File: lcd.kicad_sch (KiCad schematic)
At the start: 9 parts, among them J2 LCD 3.2" 240x320 Conn_01x14_P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, Q4 SI2301CDS-T1-GE3

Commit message: smaller caps remove ringing resistors
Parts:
- R14, R37, R38, R39: Manufacturer StackPole -> (none); Part # RMCF0603JT10K0 -> (none); VEND DIGI -> (none); VEND# RMCF0603JT10K0CT-ND -> (none)
- R3: LCSC C21190 -> C22775; Manufacturer StackPole -> (none); Part # RMCF0603JJ1K00 -> (none); VEND DIGI -> (none); VEND# RMCF0603JJ1K00CT-ND -> (none)
- R34: Manufacturer StackPole -> (none); Part # RMCF0603JJ1K00 -> (none); VEND DIGI -> (none); VEND# RMCF0603JJ1K00CT-ND -> (none)
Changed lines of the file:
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@@
 			)
 		)
-		(property "Part #" "RMCF0603JT10K0"
+		(property "Part #" ""
 			(at 77.47 -43.18 0)
 			(effects
@@
 			)
 		)
-		(property "VEND" "DIGI"
+		(property "VEND" ""
 			(at 77.47 -43.18 0)
 			(effects
@@
 			)
 		)
-		(property "VEND#" "RMCF0603JT10K0CT-ND"
+		(property "VEND#" ""
 			(at 77.47 -43.18 0)
 			(effects
@@
 			)
 		)
-		(property "Manufacturer" "StackPole"
+		(property "Manufacturer" ""
 			(at 77.47 -43.18 0)
 			(effects
@@
 			)
 		)
-		(property "LCSC" "C21190"
+		(property "LCSC" "C22775"
 			(at 119.38 104.14 0)
 			(effects
@@
 			)
 		)
-		(property "Manufacturer" "StackPole"
+		(property "Manufacturer" ""
 			(at 119.38 104.14 0)
 			(effects
@@
 			)
 		)
-		(property "Part #" "RMCF0603JJ1K00"
+		(property "Part #" ""
 			(at 119.38 104.14 0)
 			(effects
@@
 			)
 		)
-		(property "VEND" "DIGI"
+		(property "VEND" ""
 			(at 119.38 104.14 0)
 			(effects
@@
 			)
 		)
-		(property "VEND#" "RMCF0603JJ1K00CT-ND"
+		(property "VEND#" ""
 			(at 119.38 104.14 0)
 			(effects
@@
 			)
 		)
-		(property "Part #" "RMCF0603JT10K0"
+		(property "Part #" ""
 			(at 69.85 -60.96 0)
 			(effects
@@
 			)
 		)
-		(property "VEND" "DIGI"
+		(property "VEND" ""
 			(at 69.85 -60.96 0)
 			(effects
@@
 			)
 		)
-		(property "VEND#" "RMCF0603JT10K0CT-ND"
+		(property "VEND#" ""
 			(at 69.85 -60.96 0)
 			(effects
@@
 			)
 		)
-		(property "Manufacturer" "StackPole"
+		(property "Manufacturer" ""
 			(at 69.85 -60.96 0)
 			(effects
@@
 			)
 		)
-		(property "Part #" "RMCF0603JT10K0"
+		(property "Part #" ""
 			(at 16.51 8.89 0)
 			(effects
@@
 			)
 		)
-		(property "VEND" "DIGI"
+		(property "VEND" ""
 			(at 16.51 8.89 0)
 			(effects
@@
 			)
 		)
-		(property "VEND#" "RMCF0603JT10K0CT-ND"
+		(property "VEND#" ""
 			(at 16.51 8.89 0)
 			(effects
@@
 			)
 		)
-		(property "Manufacturer" "StackPole"
+		(property "Manufacturer" ""
 			(at 16.51 8.89 0)
 			(effects
@@
 			)
 		)
-		(property "Part #" "RMCF0603JT10K0"
+		(property "Part #" ""
 			(at 62.23 -60.96 0)
 			(effects
@@
 			)
 		)
-		(property "VEND" "DIGI"
+		(property "VEND" ""
 			(at 62.23 -60.96 0)
 			(effects
@@
 			)
 		)
-		(property "VEND#" "RMCF0603JT10K0CT-ND"
+		(property "VEND#" ""
 			(at 62.23 -60.96 0)
 			(effects
@@
 			)
 		)
-		(property "Manufacturer" "StackPole"
+		(property "Manufacturer" ""
 			(at 62.23 -60.96 0)
 			(effects
@@
 			)
 		)
-		(property "Manufacturer" "StackPole"
+		(property "Manufacturer" ""
 			(at 165.1 90.17 0)
 			(effects
@@
 			)
 		)
-		(property "Part #" "RMCF0603JJ1K00"
+		(property "Part #" ""
 			(at 165.1 90.17 0)
 			(effects
@@
 			)
 		)
-		(property "VEND" "DIGI"
+		(property "VEND" ""
 			(at 165.1 90.17 0)
 			(effects
@@
 			)
 		)
-		(property "VEND#" "RMCF0603JJ1K00CT-ND"
+		(property "VEND#" ""
 			(at 165.1 90.17 0)
 			(effects

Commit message: usb sheet
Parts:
- J2: now not fitted
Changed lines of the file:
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@@
 		(in_bom yes)
 		(on_board yes)
-		(dnp no)
+		(dnp yes)
 		(fields_autoplaced yes)
 		(property "Reference" "J2"

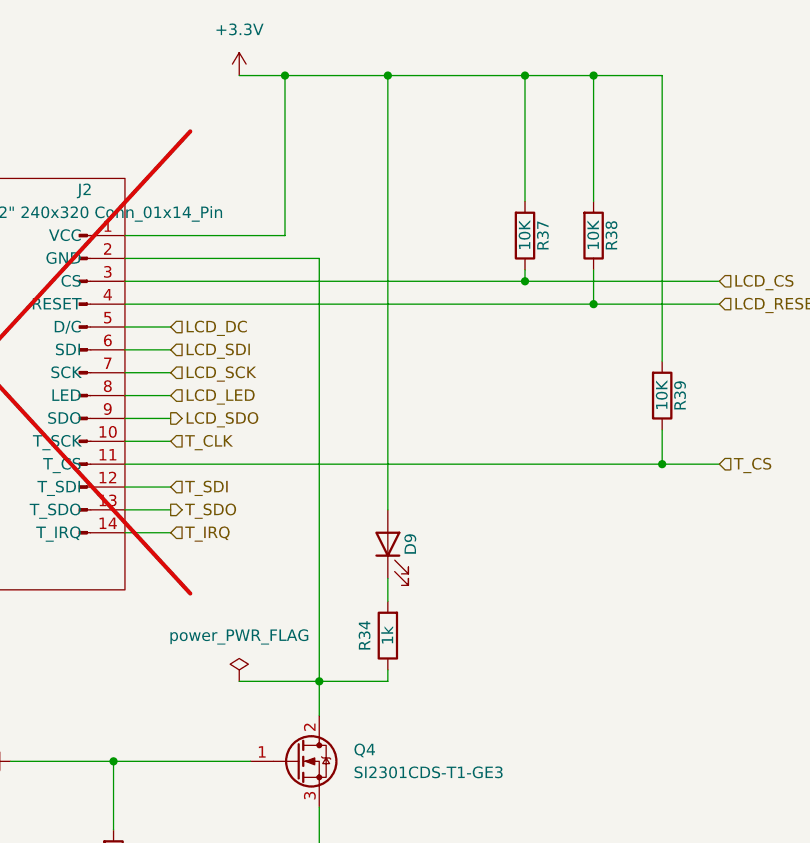
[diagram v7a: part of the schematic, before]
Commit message: smaller test pads
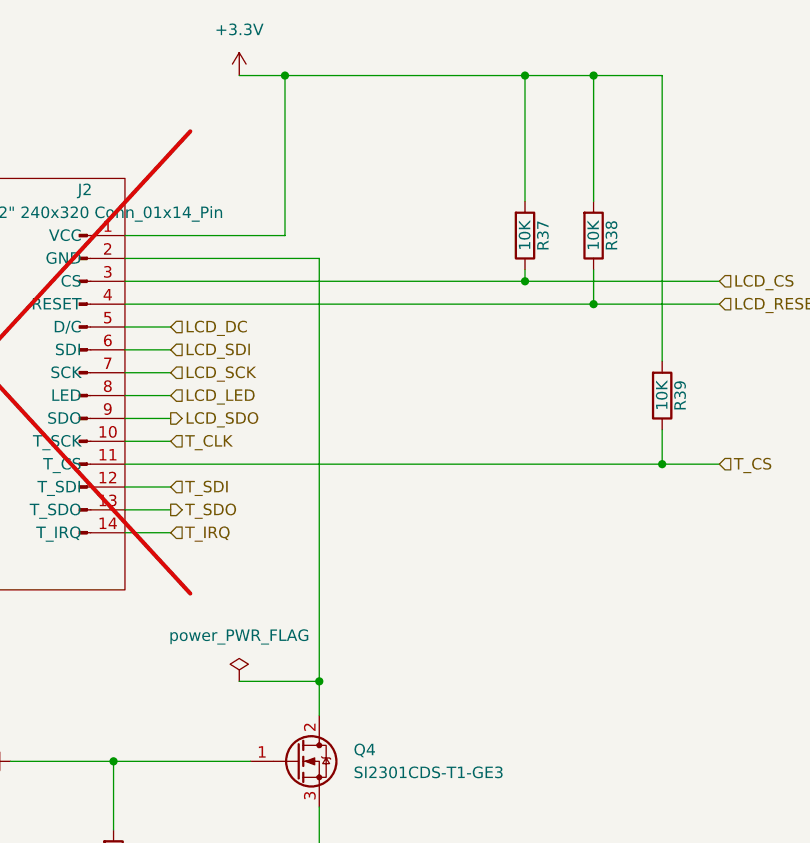
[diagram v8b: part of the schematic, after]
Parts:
- removed D9: LED-YELLOW, LED_SMD:LED_0603_1608Metric, symbol Device:LED
- removed R34: 1k, Resistor_SMD:R_0603_1608Metric, symbol Device:R
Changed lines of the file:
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@@
 	(paper "A4")
-	(junction
-		(at 165.1 27.94)
-		(diameter 0)
-		(color 0 0 0 0)
-	)
 	(junction
 		(at 187.96 27.94)
@@
 	(wire
 		(pts
-			(xy 157.48 95.25) (xy 165.1 95.25)
-		)
-		(stroke
-			(width 0)
-			(type default)
-		)
-	)
-	(wire
-		(pts
 			(xy 135.89 71.12) (xy 195.58 71.12)
 		)
@@
 	(wire
 		(pts
-			(xy 180.34 27.94) (xy 165.1 27.94)
-		)
-		(stroke
-			(width 0)
-			(type default)
-		)
-	)
-	(wire
-		(pts
 			(xy 135.89 76.2) (xy 140.97 76.2)
 		)
@@
 	(wire
 		(pts
-			(xy 165.1 93.98) (xy 165.1 95.25)
-		)
-		(stroke
-			(width 0)
-			(type default)
-		)
-	)
-	(wire
-		(pts
 			(xy 134.62 104.14) (xy 134.62 111.76)
 		)
@@
 	(wire
 		(pts
-			(xy 165.1 27.94) (xy 165.1 76.2)
-		)
-		(stroke
-			(width 0)
-			(type default)
-		)
-	)
-	(wire
-		(pts
 			(xy 153.67 27.94) (xy 153.67 45.72)
 		)
@@
 	(wire
 		(pts
-			(xy 153.67 27.94) (xy 165.1 27.94)
+			(xy 153.67 27.94) (xy 180.34 27.94)
 		)
 		(stroke
@@
 		(pts
 			(xy 195.58 71.12) (xy 201.93 71.12)
-		)
-		(stroke
-			(width 0)
-			(type default)
-		)
-	)
-	(wire
-		(pts
-			(xy 165.1 83.82) (xy 165.1 86.36)
 		)
 		(stroke
@@
 			)
 		)
+		(property "Silkscreen" ""
+			(at 195.58 63.5 0)
+			(effects
+				(font
+					(size 1.27 1.27)
+				)
+				(hide yes)
+			)
+		)
 		(pin "1"
 		)
@@
 				(path "/8d063f79-9282-4820-bcf4-1ff3c006cf08/98bf8f66-79b9-41fc-9cd7-550fbae3319a"
 					(reference "R39")
-					(unit 1)
-				)
-			)
-		)
-	)
-	(symbol
-		(lib_id "Device:LED")
-		(at 165.1 80.01 90)
-		(unit 1)
-		(exclude_from_sim no)
-		(in_bom yes)
-		(on_board yes)
-		(dnp no)
-		(property "Reference" "D9"
-			(at 167.64 80.01 0)
-			(effects
-				(font
-					(size 1.27 1.27)
-				)
-			)
-		)
-		(property "Value" "LED-YELLOW"
-			(at 162.56 82.55 0)
-			(effects
-				(font
-					(size 1.27 1.27)
-				)
-				(hide yes)
-			)
-		)
-		(property "Footprint" "LED_SMD:LED_0603_1608Metric"
-			(at 165.1 80.01 0)
-			(effects
-				(font
-					(size 1.524 1.524)
-				)
-				(hide yes)
-			)
-		)
-		(property "Datasheet" "https://wmsc.lcsc.com/wmsc/upload/file/pdf/v2/lcsc/1810101813_Everlight-Elec-19-213-Y2C-CQ2R2L-3T-CY_C72038.pdf"
-			(at 165.1 80.01 0)
-			(effects
-				(font
-					(size 1.524 1.524)
-				)
-				(hide yes)
-			)
-		)
-		(property "Description" "Light emitting diode"
-			(at 165.1 80.01 0)
-			(effects
-				(font
-					(size 1.27 1.27)
-				)
-				(hide yes)
-			)
-		)
-		(property "LCSC" "C72038"
-			(at 165.1 80.01 0)
-			(effects
-				(font
-					(size 1.27 1.27)
-				)
-				(hide yes)
-			)
-		)
-		(property "Sim.Device" ""
-			(at 165.1 80.01 0)
-			(effects
-				(font
-					(size 1.27 1.27)
-				)
-				(hide yes)
-			)
-		)
-		(property "Sim.Pins" ""
-			(at 165.1 80.01 0)
-			(effects
-				(font
-					(size 1.27 1.27)
-				)
-				(hide yes)
-			)
-		)
-		(pin "1"
-		)
-		(pin "2"
-		)
-		(instances
-			(project "l8-kicad"
-				(path "/8d063f79-9282-4820-bcf4-1ff3c006cf08/98bf8f66-79b9-41fc-9cd7-550fbae3319a"
-					(reference "D9")
 					(unit 1)
 				)
@@
 		)
 		(property "Sim.Pins" ""
+			(at 119.38 104.14 0)
+			(effects
+				(font
+					(size 1.27 1.27)
+				)
+				(hide yes)
+			)
+		)
+		(property "Silkscreen" ""
 			(at 119.38 104.14 0)
 			(effects
@@
 			)
 		)
+		(property "Silkscreen" ""
+			(at 187.96 45.72 0)
+			(effects
+				(font
+					(size 1.27 1.27)
+				)
+				(hide yes)
+			)
+		)
 		(pin "1"
 		)
@@
 			)
 		)
+		(property "Silkscreen" ""
+			(at 134.62 115.57 0)
+			(effects
+				(font
+					(size 1.27 1.27)
+				)
+				(hide yes)
+			)
+		)
 		(pin "1"
 		)
@@
 			)
 		)
+		(property "Silkscreen" ""
+			(at 154.94 104.14 0)
+			(effects
+				(font
+					(size 1.27 1.27)
+				)
+				(hide yes)
+			)
+		)
 		(pin "2"
 		)
@@
 		)
 		(property "Sim.Pins" ""
+			(at 130.81 60.96 0)
+			(effects
+				(font
+					(size 1.27 1.27)
+				)
+				(hide yes)
+			)
+		)
+		(property "Silkscreen" ""
 			(at 130.81 60.96 0)
 			(effects
@@
 			)
 		)
+		(property "Silkscreen" ""
+			(at 180.34 45.72 0)
+			(effects
+				(font
+					(size 1.27 1.27)
+				)
+				(hide yes)
+			)
+		)
 		(pin "1"
 		)
@@
 					(unit 1)
 				)
-			)
-		)
-	)
-	(symbol
-		(lib_id "Device:R")
-		(at 165.1 90.17 180)
-		(unit 1)
-		(exclude_from_sim no)
-		(in_bom yes)
-		(on_board yes)
-		(dnp no)
-		(property "Reference" "R34"
-			(at 162.56 90.17 90)
-			(effects
-				(font
-					(size 1.27 1.27)
-				)
-			)
-		)
-		(property "Value" "1k"
-			(at 165.1 90.17 90)
-			(effects
-				(font
-					(size 1.27 1.27)
-				)
-			)
-		)
-		(property "Footprint" "Resistor_SMD:R_0603_1608Metric"
-			(at 166.878 90.17 90)
-			(effects
-				(font
-					(size 1.27 1.27)
-				)
-				(hide yes)
-			)
-		)
-		(property "Datasheet" "~"
-			(at 165.1 90.17 0)
-			(effects
-				(font
-					(size 1.27 1.27)
-				)
-				(hide yes)
-			)
-		)
-		(property "Description" "Resistor"
-			(at 165.1 90.17 0)
-			(effects
-				(font
-					(size 1.27 1.27)
-				)
-				(hide yes)
-			)
-		)
-		(property "LCSC" "C21190"
-			(at 165.1 90.17 0)
-			(effects
-				(font
-					(size 1.27 1.27)
-				)
-				(hide yes)
-			)
-		)
-		(property "Manufacturer" ""
-			(at 165.1 90.17 0)
-			(effects
-				(font
-					(size 1.27 1.27)
-				)
-				(hide yes)
-			)
-		)
-		(property "Part #" ""
-			(at 165.1 90.17 0)
-			(effects
-				(font
-					(size 1.27 1.27)
-				)
-				(hide yes)
-			)
-		)
-		(property "VEND" ""
-			(at 165.1 90.17 0)
-			(effects
-				(font
-					(size 1.27 1.27)
-				)
-				(hide yes)
-			)
-		)
-		(property "VEND#" ""
-			(at 165.1 90.17 0)
-			(effects
-				(font
-					(size 1.27 1.27)
-				)
-				(hide yes)
-			)
-		)
-		(property "Sim.Device" ""
-			(at 165.1 90.17 0)
-			(effects
-				(font
-					(size 1.27 1.27)
-				)
-				(hide yes)
-			)
-		)
-		(property "Sim.Pins" ""
-			(at 165.1 90.17 0)
-			(effects
-				(font
-					(size 1.27 1.27)
-				)
-				(hide yes)
-			)
-		)
-		(pin "1"
-		)
-		(pin "2"
-		)
-		(instances
-			(project "l8-kicad"
-				(path "/8d063f79-9282-4820-bcf4-1ff3c006cf08/98bf8f66-79b9-41fc-9cd7-550fbae3319a"
-					(reference "R34")
-					(unit 1)
-				)
